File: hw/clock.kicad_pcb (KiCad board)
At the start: 2 copper layers, 109.9 x 52.5 mm, 70 parts, among them J1 USB-A1HSW6, J2 USB-A1HSW6, J3 USB-A1HSW6, SW1 TL3305AF260QG, SW2 TL3305AF260QG, SW3 TL3305AF260QG, U1 LPC812M101JDH20, U10 HDSP-5321 Common Anode, U11 HDSP-5321 Common Anode, U12 HDSP-5321 Common Anode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

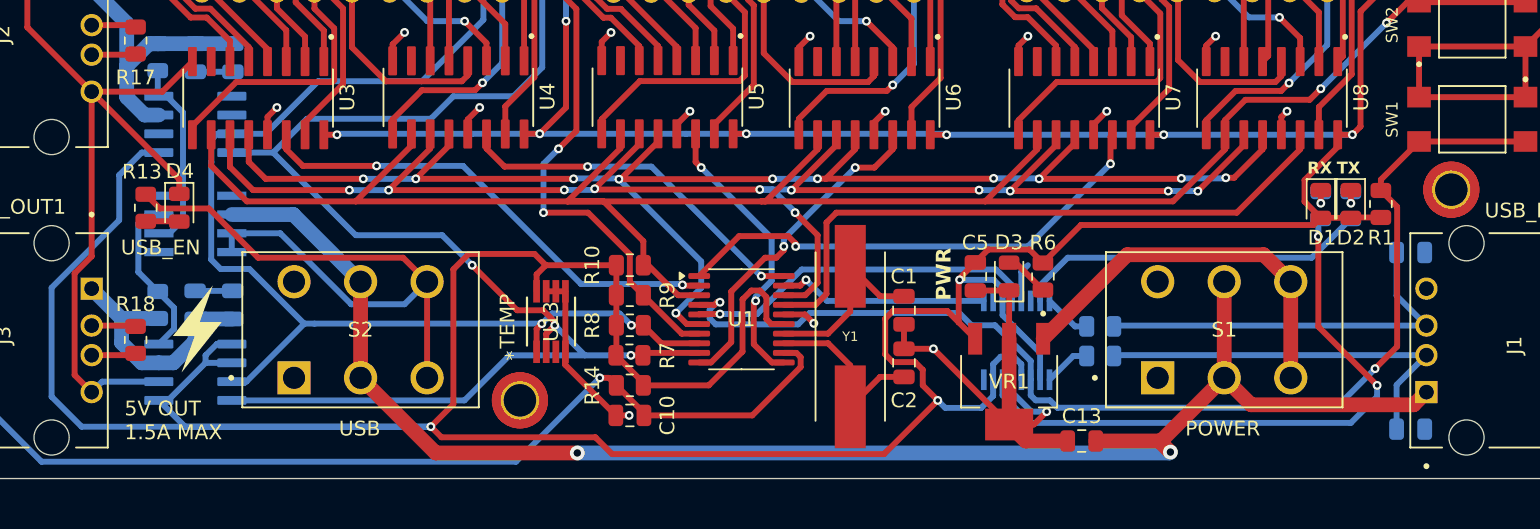
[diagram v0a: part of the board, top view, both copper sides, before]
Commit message: Move temp sensor, add quote
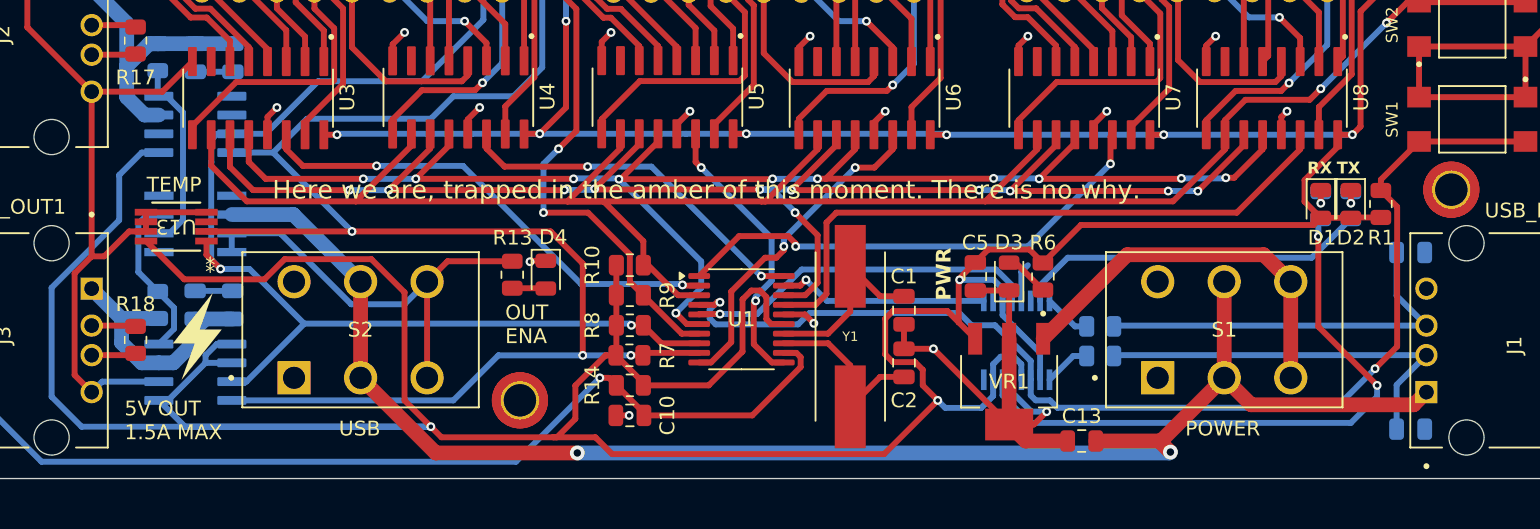
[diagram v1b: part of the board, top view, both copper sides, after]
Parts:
- moved U13 26.2 mm to (155.8, 83.8), turned to 180 degrees
- moved D4 25.2 mm to (180.8, 87.0)
- moved R13 25.2 mm to (178.5, 87.0)
- moved G*** 0.50 mm to (157.0, 91.0)
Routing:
- net Net-(U14-EN1): track 45.1 -> 29.9 mm
- net +3V3: track 350.9 -> 363.6 mm
- net SCL: track 99.0 -> 110.2 mm
- net GND: track 186.6 -> 176.1 mm, vias 15 -> 16
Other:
- board text added: "Here we are, trapped in the amber of this moment. There is no why."
- board text added: "Ian Feldman 2025"
- board text added: "JLCJLCJLCJLC"
- board text added: "OUT ENA"
- board text removed: "USB_EN"

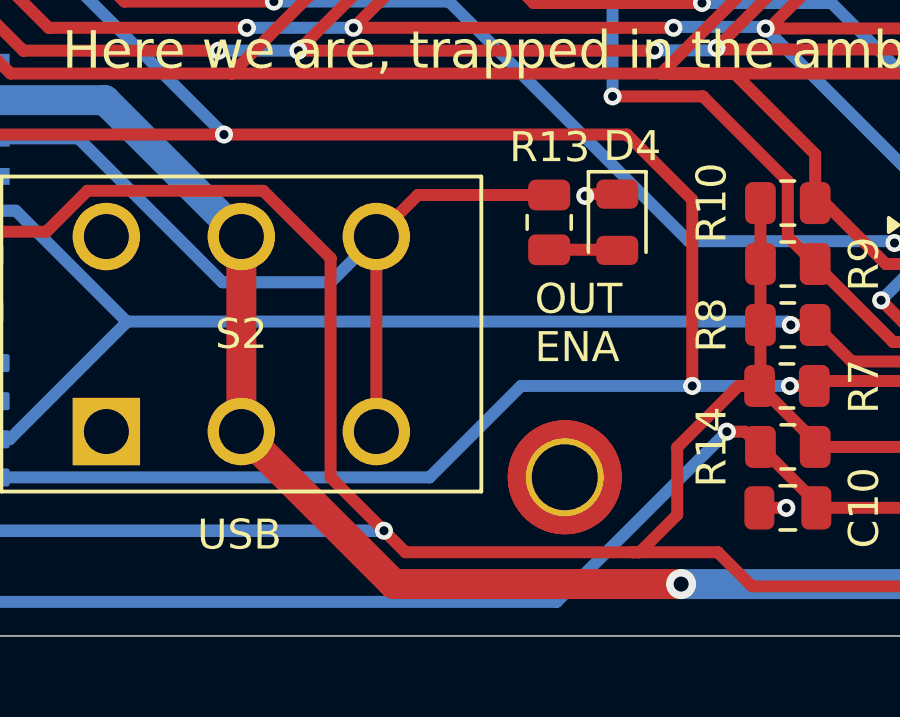
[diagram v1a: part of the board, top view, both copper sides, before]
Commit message: Add pull load switch pull down
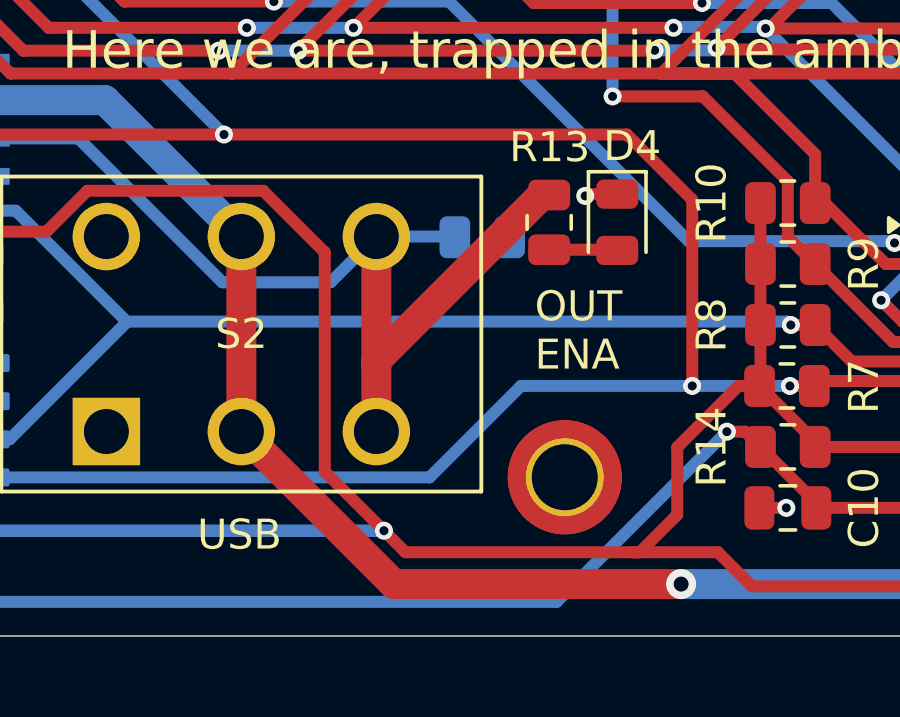
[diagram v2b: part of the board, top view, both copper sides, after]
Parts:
- added R19: 10k, Resistor_SMD:R_0805_2012Metric, B.Cu at (176.2, 87.5)
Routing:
- net Net-(U14-EN1): track 29.9 -> 34.4 mm

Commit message: Add safety resistors and 5v display backup supply
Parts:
- added R20: 0, Resistor_SMD:R_0805_2012Metric, B.Cu at (207.0, 89.4)
- added R21: 15, Resistor_SMD:R_0805_2012Metric, F.Cu at (246.5, 65.0)
- moved R11 0.48 mm to (243.0, 65.0)
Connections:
- U2 pad 10: +3V3 -> Net-(U2-3V3OUT)
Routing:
- net +5V: track 106.8 -> 141.5 mm
- net Net-(U2-3V3OUT): track 0.00 -> 9.62 mm
- net +3V3: track 363.6 -> 359.1 mm
- net Net-(R11-Pad1): track 7.47 -> 9.76 mm
- net GND: track 176.1 -> 174.6 mm
- net SERIAL2: track 23.9 -> 25.2 mm
- net SCL: track 110.2 -> 111.3 mm
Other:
- board text added: "3V3"
- board text added: "5V"
